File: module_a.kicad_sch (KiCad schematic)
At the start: 27 parts, among them J6 Micro_SD_Card_Det2, J7 nRPIBOOT Jumper, U3 TPD4EUSB30, U4 TPD4EUSB30, U5 MAX3232, U6 RT9742GGJ5

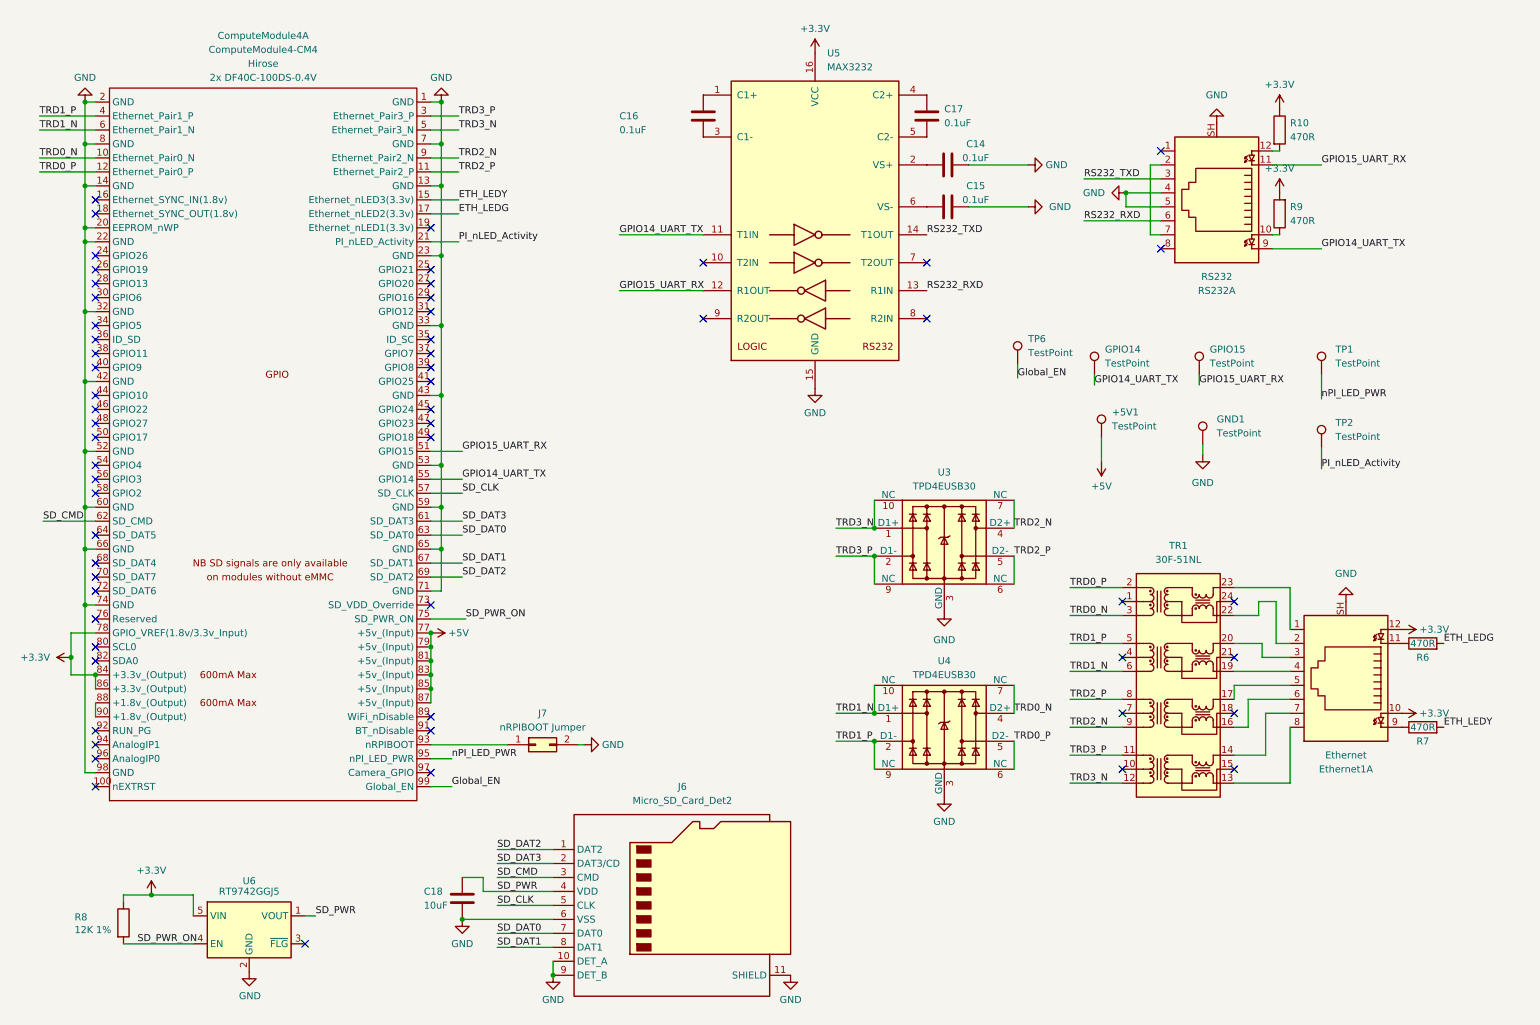
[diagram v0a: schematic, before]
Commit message: Fix ethernet wiring order
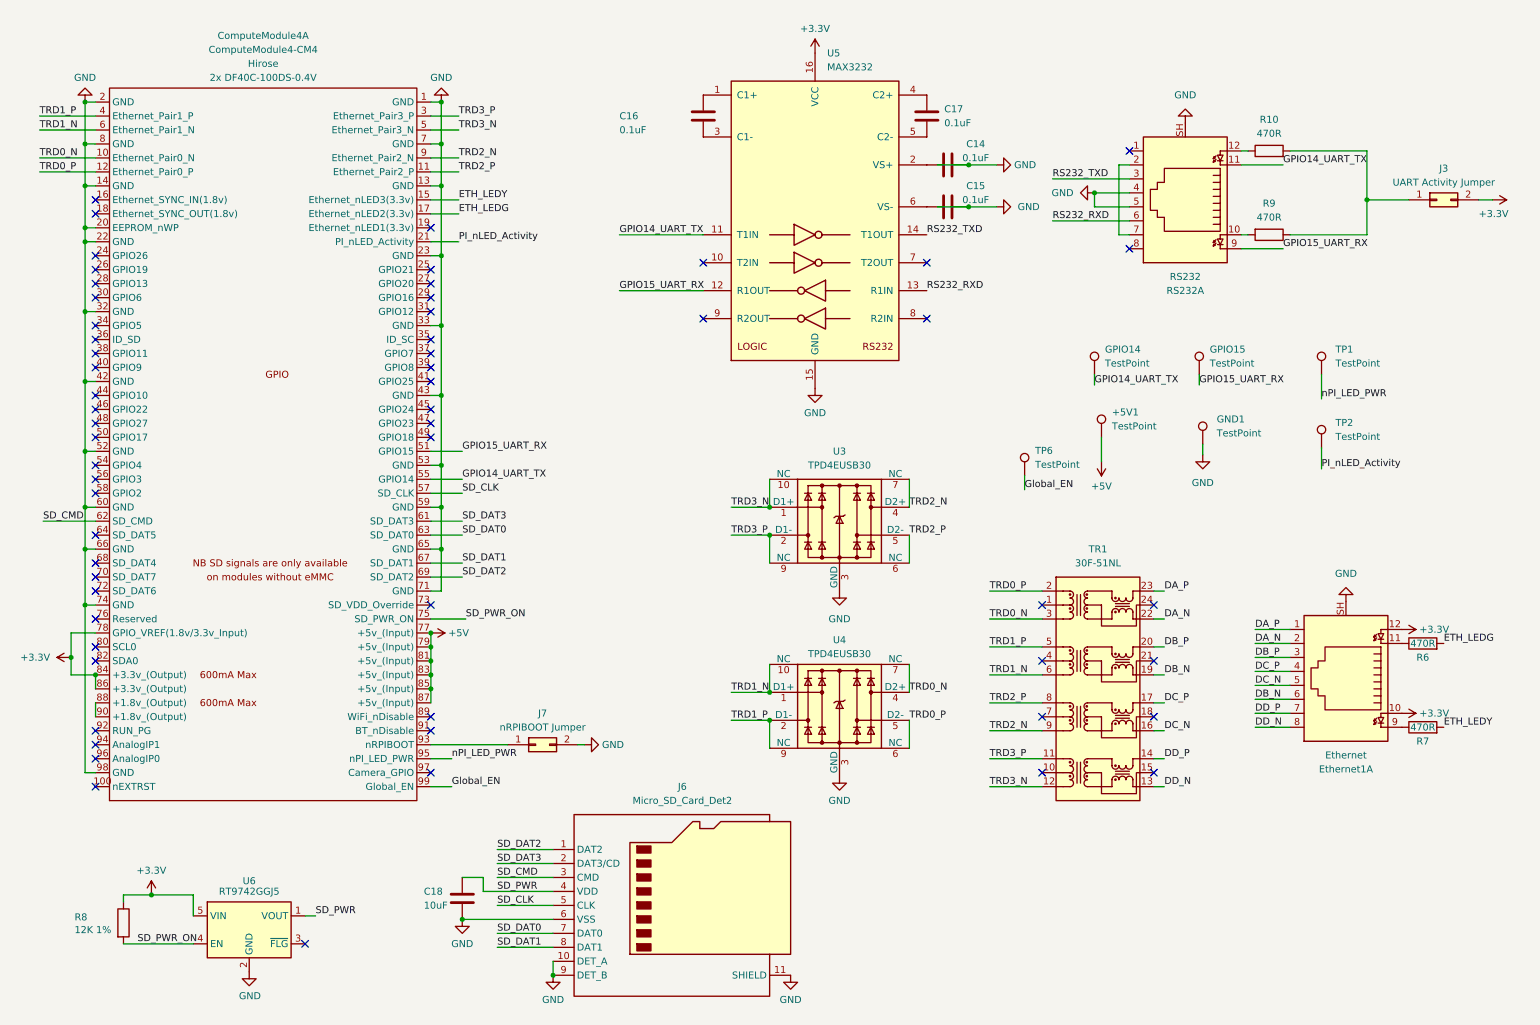
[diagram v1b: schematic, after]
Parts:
- added J3: UART Activity Jumper, Connector_PinHeader_2.00mm:PinHeader_1x02_P2.00mm_Vertical, symbol Connector_Generic:Conn_02x01
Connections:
- net +3.3V: now also J3.2 (Pin_2); no longer R10.1, R9.2
- net GPIO14_UART_TX: now also RS232.11; no longer RS232.9
- net GPIO15_UART_RX: now also RS232.9; no longer RS232.11
- net DA_P: now reaches Ethernet1.1, TR1.23 (MX1+)
- net DA_N: now reaches Ethernet1.2, TR1.22 (MX1-)
- net DB_P: now reaches Ethernet1.3, TR1.20 (MX2+)
- net DB_N: now reaches TR1.19 (MX2-)
- net DB_N: now also Ethernet1.6; no longer Ethernet1.4
- net DC_N: now reaches Ethernet1.5
- net DC_N: now also TR1.16 (MX3-); no longer TR1.17 (MX3+)
- net DD_P: now reaches Ethernet1.7, TR1.14 (MX4+)
- net DD_N: now reaches Ethernet1.8, TR1.13 (MX4-)
- net at RS232.10: now also R9.2; no longer R9.1
- net at RS232.12: now also R10.1; no longer R10.2
- new net: J3.1 (Pin_1), R10.2, R9.1
- new net DC_P: Ethernet1.4, TR1.17 (MX3+)
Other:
- moved on the sheet: R10, R9, RS232A, TP6, TR1, U3, U4

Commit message: Clean up schematics
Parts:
- C14, C15, C16, C17: value 0.1uF -> 100nF
- renumbered Ethernet1 to J5, RS232 to J8

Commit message: PiCard v2
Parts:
- removed +5V1, GND1, GPIO14, GPIO15, TP1, TP2, TP6: TestPoint, TestPoint:TestPoint_Pad_D2.0mm, symbol Connector:TestPoint
- removed J3: UART Activity Jumper, Connector_PinHeader_2.00mm:PinHeader_1x02_P2.00mm_Vertical, symbol Connector_Generic:Conn_02x01
- removed J7: nRPIBOOT Jumper, Connector_PinHeader_2.00mm:PinHeader_1x02_P2.00mm_Vertical, symbol Connector_Generic:Conn_02x01
- removed TR1: 30F-51NL, Transformer_SMD:Transformer_Ethernet_YDS_30F-51NL_SO-24_7.1x15.1mm, symbol Transformer:30F-51NL
- removed U6: RT9742GGJ5, Package_TO_SOT_SMD:TSOT-23-5, symbol PiCard:RT9742GGJ5F
- added C1, C34, C7: 100n, Capacitor_SMD:C_0402_1005Metric, symbol Device:C
- added C6, C8: 1u, Capacitor_SMD:C_0603_1608Metric, symbol Device:C
- added D1, D3: 1N5819WS, Diode_SMD:D_SOD-323, symbol Device:D_Schottky
- added D4: LED_Dual_AAKK, PiCard:LED-ARRAY-SMD_4P-L3.0-W1.5-L-FD, symbol Device:LED_Dual_AAKK
- added R21: 15.8k, Resistor_SMD:R_0402_1005Metric, symbol Device:R
- added R3, R36: 1k, Resistor_SMD:R_0402_1005Metric, symbol Device:R
- added R4, R5: 100k 1%, Resistor_SMD:R_0402_1005Metric, symbol Device:R
- added TR1: H2456G, PiCard:XFMR-SMD-24_L16.6-W9.0-LS9.6-BL, symbol Magi:H2456G
- added U18: 74LVC1G07, Package_TO_SOT_SMD:SOT-353_SC-70-5, symbol 74xGxx:74LVC1G07
- added U2: SN74AHC123A, Package_SO:TSSOP-16_4.4x5mm_P0.65mm, symbol 74xx:74AHCT123
- added U5: ~, Package_TO_SOT_SMD:SOT-23-6, symbol PiCard:TPS2553
- C2: renamed from C16; value 100nF -> 100n; footprint Capacitor_SMD:C_0603_1608Metric -> Capacitor_SMD:C_0402_1005Metric; LCSC C45000 -> C307331; MPN (none) -> CL05B104KB54PNC; Manufacturer (none) -> Samsung
- C3: renamed from C17; value 100nF -> 100n; footprint Capacitor_SMD:C_0603_1608Metric -> Capacitor_SMD:C_0402_1005Metric; LCSC C45000 -> C307331; MPN (none) -> CL05B104KB54PNC; Manufacturer (none) -> Samsung
- C4: renamed from C14; value 100nF -> 100n; footprint Capacitor_SMD:C_0603_1608Metric -> Capacitor_SMD:C_0402_1005Metric; LCSC C45000 -> C307331; MPN (none) -> CL05B104KB54PNC; Manufacturer (none) -> Samsung
- C5: renamed from C15; value 100nF -> 100n; footprint Capacitor_SMD:C_0603_1608Metric -> Capacitor_SMD:C_0402_1005Metric; LCSC C45000 -> C307331; MPN (none) -> CL05B104KB54PNC; Manufacturer (none) -> Samsung
- C9: renamed from C18; value 10uF -> 10u; LCSC C2167686 -> C15850; MPN (none) -> CL21A106KAYNNNE; Manufacturer (none) -> C15850
- J1: renamed from J8; footprint PiCard:RJ45-TH_MJ88B-B011-RVL11-P -> PiCard:RJ45-TH_RJ45-005-202-11; symbol Connector:RJ45_LED_Shielded_x2 -> Connector:RJ45_LED_Shielded; LCSC C501462 -> C7421405; MPN (none) -> RJ45-005-202-11; Manufacturer (none) -> Heling
- J2: renamed from J5; footprint PiCard:RJ45-TH_MJ88B-B011-RVL11-P -> PiCard:RJ45-TH_RJ45-005-202-11; symbol Connector:RJ45_LED_Shielded_x2 -> Connector:RJ45_LED_Shielded; LCSC C501462 -> C7421405; MPN (none) -> RJ45-005-202-11; Manufacturer (none) -> Heling
- J3: renamed from J6; LCSC (none) -> C5174683; LCSC Part # C5174683 -> (none); MPN (none) -> TF-108-ARP10; Manufacturer (none) -> XUNPU
- R1: renamed from R10; value 470R -> 470; footprint Resistor_SMD:R_0805_2012Metric -> Resistor_SMD:R_0402_1005Metric; LCSC C17710 -> C25117; MPN (none) -> 0402WGF4700TCE; Manufacturer (none) -> Uniroyal
- R2: renamed from R9; value 470R -> 470; footprint Resistor_SMD:R_0805_2012Metric -> Resistor_SMD:R_0402_1005Metric; LCSC C17710 -> C25117; MPN (none) -> 0402WGF4700TCE; Manufacturer (none) -> Uniroyal
- R6, R7: value 470R -> 470; footprint Resistor_SMD:R_0805_2012Metric -> Resistor_SMD:R_0402_1005Metric; LCSC C17710 -> C25117; MPN (none) -> 0402WGF4700TCE; Manufacturer (none) -> Uniroyal
- R8: value 12K 1% -> 12k; footprint Resistor_SMD:R_0805_2012Metric -> Resistor_SMD:R_0402_1005Metric; LCSC C17444 -> C25752; MPN (none) -> 0402WGF1202TCE; Manufacturer (none) -> Uniroyal
- U1: renamed from U5; footprint PiCard:TSSOP-16_L5.0-W4.4-P0.65-LS6.4-BL -> Package_SO:TSSOP-16_4.4x5mm_P0.65mm; MPN (none) -> MAX3232EEUE+T; Manufacturer (none) -> Maxim
- U3, U4: MPN (none) -> TPD4EUSB30DQAR; Manufacturer (none) -> Texas Instruments
- renumbered ComputeModule4 to ComputeModule1
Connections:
- net +3.3V: now also R8.2, C1.2, C34.2, C7.2, D1.1 (K), D3.1 (K), D4.1 (A1), D4.2 (A2), R4.1, R5.1, U18.5 (VCC), U2.10 (B), U2.16 (VCC), U2.2 (B), U5.1 (IN); no longer R8.1
- net DA_N: now also TR1.2 (MX1+)
- net DA_P: now also TR1.3 (MX1-)
- net DB_N: now also TR1.5 (MX2+)
- net DB_P: now also TR1.6 (MX2-)
- net DC_N: now also TR1.8 (MX3+)
- net DC_P: now also TR1.9 (MX3-)
- net DD_N: now also TR1.11 (MX4+)
- net DD_P: now also TR1.12 (MX4-)
- net GND: now also J1.11, J1.9, C1.1, C34.1, C6.2, C7.1, C8.2, R21.2, U18.3 (GND), U2.14 (Cext), U2.6 (Cext), U2.8 (GND), U5.2 (GND); no longer ComputeModule1.98 (GND)
- net GPIO14_UART_TX: now also U2.1 (A); no longer J1.11
- net GPIO15_UART_RX: now also U2.9 (A); no longer J1.9
- net SD_PWR: now also U5.6 (OUT)
- net SD_PWR_ON: now also R8.1, U5.3 (EN); no longer R8.2
- net TRD0_N: now also U4.1 (D1+), U4.10 (NC), TR1.23 (TD1+); no longer U4.4 (D2+), U4.7 (NC)
- net TRD0_P: now also U4.2 (D1-), U4.9 (NC), TR1.22 (TD1-); no longer U4.5 (D2-), U4.6 (NC)
- net TRD1_N: now also U4.4 (D2+), U4.7 (NC), TR1.20 (TD2+); no longer U4.1 (D1+), U4.10 (NC)
- net TRD1_P: now also U4.5 (D2-), U4.6 (NC), TR1.19 (TD2-); no longer U4.2 (D1-), U4.9 (NC)
- net TRD2_N: now also U3.5 (D2-), U3.6 (NC), TR1.17; no longer U3.4 (D2+), U3.7 (NC)
- net TRD2_P: now also U3.4 (D2+), U3.7 (NC), TR1.16 (TD3-); no longer U3.5 (D2-), U3.6 (NC)
- net TRD3_N: now also U3.2 (D1-), U3.9 (NC), TR1.14 (TD4+); no longer U3.1 (D1+), U3.10 (NC)
- net TRD3_P: now also U3.1 (D1+), U3.10 (NC), TR1.13 (TD4-); no longer U3.2 (D1-), U3.9 (NC)
- net RTC_SCL: now reaches ComputeModule1.56 (GPIO3)
- net RTC_SDA: now reaches ComputeModule1.58 (GPIO2)
- net RPIBOOT: now reaches ComputeModule1.93 (nRPIBOOT)
- net UART_RX_ACT: now reaches R2.1
- net UART_RX_ACT: now also U2.5 (Q); no longer R1.2
- net Global_EN: no longer names the net of ComputeModule1.99 (Global_EN)
- net PI_nLED_Activity renamed GREEN_LED_K
- net GREEN_LED_K: now also R3.1
- net nPI_LED_PWR: no longer names the net of ComputeModule1.95 (nPI_LED_PWR)
- net nPI_LED_PWR: now also U18.2
- new net: R21.1, U5.5 (ILM)
- new net: C6.1, D1.2 (A), R4.2, U2.15 (RCext)
- new net: C8.1, D3.2 (A), R5.2, U2.7 (RCext)
- new net: D4.3 (K1), R36.2
- new net: D4.4 (K2), R3.2
- new net RED_LED_K: R36.1, U18.4
- new net UART_ACT_EN: U2.11 (Clr), U2.3 (Clr)
- new net UART_TX_ACT: R1.2, U2.13 (Q)
- no-connect marks 59 -> 62
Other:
- moved on the sheet: C9, ComputeModule1A, J1, J3, R1, R2, U3, U4

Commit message: PiCard v2.2
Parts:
- U5: value ~ -> TPS2553
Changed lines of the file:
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@@
 			)
 		)
-		(property "Value" "~"
+		(property "Value" "TPS2553"
 			(at 45.72 170.815 0)
 			(effects

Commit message: wip
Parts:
- removed C5: 100n, Capacitor_SMD:C_0402_1005Metric, symbol Device:C
- removed D4: LED_Dual_AAKK, PiCard:LED-ARRAY-SMD_4P-L3.0-W1.5-L-FD, symbol Device:LED_Dual_AAKK
- removed R3, R36: 1k, Resistor_SMD:R_0402_1005Metric, symbol Device:R
- removed U1: MAX3232, Package_SO:TSSOP-16_4.4x5mm_P0.65mm, symbol Interface_UART:MAX3232
- removed U18: 74LVC1G07, Package_TO_SOT_SMD:SOT-353_SC-70-5, symbol 74xGxx:74LVC1G07
- added U1: ADM3101EACPZ, PiCard:LFCSP-12-1EP_3x3mm_P0.5mm_EP1.3x1.3mm, symbol PiCard:ADM3101EACPZ
- U2: footprint Package_SO:TSSOP-16_4.4x5mm_P0.65mm -> Package_DFN_QFN:DHVQFN-16-1EP_2.5x3.5mm_P0.5mm_EP1x2mm
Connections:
- net +3.3V: no longer C1.2
- net GND: now also U1.13 (GND), U1.6 (GND); no longer C1.1
- net GPIO14_UART_TX: now also U1.3 (TIN)
- net GPIO15_UART_RX: now also U1.2 (ROUT)
- net RS232_RXD: now also U1.8 (TOUT)
- net RS232_TXD: now also U1.9 (RIN)
- net at C2.1: now also U1.11 (C2+)
- net at C4.1: now also U1.7 (V-)
- net at C2.2: now also U1.10 (C2-)
- net at C3.1: now also U1.5 (VCC)
- net at C3.2: now also U1.4 (V+)
- new net: C1.1, U1.1 (C1+)
- new net: C1.2, U1.12 (C1-)
- no-connect marks 62 -> 57
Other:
- moved on the sheet: C6, C7, C8, D1, D3, J1, J2, R1, R2, R4, R5, R6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

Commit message: wip2
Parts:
- U2: value SN74AHC123A -> 74AHCT123ABQ; LCSC C2869599 -> C554491; MPN SN74AHC123APWR -> 74AHCT123ABQ,115; Manufacturer Texas Instruments -> Nexperia
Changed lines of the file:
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@@
 			)
 		)
-		(property "Value" "SN74AHC123A"
+		(property "Value" "74AHCT123ABQ"
 			(at 268.605 83.82 0)
 			(effects
@@
 			)
 		)
-		(property "Datasheet" "https://www.ti.com/lit/ds/symlink/sn74ahc123a.pdf"
+		(property "Datasheet" "https://assets.nexperia.com/documents/data-sheet/74AHC_AHCT123A.pdf"
 			(at 261.62 82.55 0)
 			(effects
@@
 			)
 		)
-		(property "LCSC" "C2869599"
+		(property "LCSC" "C554491"
 			(at 261.62 82.55 0)
 			(effects
@@
 			)
 		)
-		(property "MPN" "SN74AHC123APWR"
+		(property "MPN" "74AHCT123ABQ,115"
 			(at 261.62 82.55 0)
 			(effects
@@
 			)
 		)
-		(property "Manufacturer" "Texas Instruments"
+		(property "Manufacturer" "Nexperia"
 			(at 261.62 82.55 0)
 			(effects
@@
 			)
 		)
-		(property "Value" "SN74AHC123A"
+		(property "Value" "74AHCT123ABQ"
 			(at 228.6 76.2 0)
 			(effects
@@
 			)
 		)
-		(property "Datasheet" "https://www.ti.com/lit/ds/symlink/sn74ahc123a.pdf"
+		(property "Datasheet" "https://assets.nexperia.com/documents/data-sheet/74AHC_AHCT123A.pdf"
 			(at 228.6 86.36 0)
 			(effects
@@
 			)
 		)
-		(property "LCSC" "C2869599"
+		(property "LCSC" "C554491"
 			(at 228.6 86.36 0)
 			(effects
@@
 			)
 		)
-		(property "MPN" "SN74AHC123APWR"
+		(property "MPN" "74AHCT123ABQ,115"
 			(at 228.6 86.36 0)
 			(effects
@@
 			)
 		)
-		(property "Manufacturer" "Texas Instruments"
+		(property "Manufacturer" "Nexperia"
 			(at 228.6 86.36 0)
 			(effects
@@
 			)
 		)
-		(property "Value" "SN74AHC123A"
+		(property "Value" "74AHCT123ABQ"
 			(at 165.1 76.835 0)
 			(effects
@@
 			)
 		)
-		(property "Datasheet" "https://www.ti.com/lit/ds/symlink/sn74ahc123a.pdf"
+		(property "Datasheet" "https://assets.nexperia.com/documents/data-sheet/74AHC_AHCT123A.pdf"
 			(at 165.1 86.36 0)
 			(effects
@@
 			)
 		)
-		(property "LCSC" "C2869599"
+		(property "LCSC" "C554491"
 			(at 165.1 86.36 0)
 			(effects
@@
 			)
 		)
-		(property "MPN" "SN74AHC123APWR"
+		(property "MPN" "74AHCT123ABQ,115"
 			(at 165.1 86.36 0)
 			(effects
@@
 			)
 		)
-		(property "Manufacturer" "Texas Instruments"
+		(property "Manufacturer" "Nexperia"
 			(at 165.1 86.36 0)
 			(effects

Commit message: wip3
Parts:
- removed C34: 100n, Capacitor_SMD:C_0402_1005Metric, symbol Device:C
- removed R21: 15.8k, Resistor_SMD:R_0402_1005Metric, symbol Device:R
- removed U5: TPS2553, Package_TO_SOT_SMD:SOT-23-6, symbol PiCard:TPS2553
- added U18: TPS2069C, Package_TO_SOT_SMD:SOT-23-5, symbol PiCard:TPS2069C
- J3: footprint PiCard:TF-SMD_503398-1892 -> PiCard:SDCARD_MOLEX_503398-1892; LCSC C5174683 -> C428492; MPN TF-108-ARP10 -> 5033981892; Manufacturer XUNPU -> MOLEX
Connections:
- net +3.3V: now also U18.5 (IN)
- net GND: now also U18.2 (GND)
- net RS232_RXD: now also U1.9 (RIN); no longer U1.8 (TOUT)
- net RS232_TXD: now also U1.8 (TOUT); no longer U1.9 (RIN)
- net SD_PWR: now also U18.1 (OUT)
- net SD_PWR_ON: now also U18.4 (EN)
- net MCU_nRST: now reaches ComputeModule1.24 (GPIO26)
- net CM_SPI1_SCLK: now reaches ComputeModule1.25 (GPIO21)
- net CM_SPI1_SIO1: now reaches ComputeModule1.26 (GPIO19)
- net CM_SPI1_SIO0: now reaches ComputeModule1.27 (GPIO20)
- net CM_UART4_RX: now reaches ComputeModule1.28 (GPIO13)
- net MCU_SWDCLK: now reaches ComputeModule1.30 (GPIO6)
- net CM_UART4_TX: now reaches ComputeModule1.31 (GPIO12)
- net CM_I2C2_SCL: now reaches ComputeModule1.34 (GPIO5)
- net CM_ID_SC: now reaches ComputeModule1.35 (ID_SC)
- net CM_ID_SD: now reaches ComputeModule1.36 (ID_SD)
- net MCU_SWDIO: now reaches ComputeModule1.37 (GPIO7)
- net CM_UART3_TX: now reaches ComputeModule1.39 (GPIO8)
- net CM_UART3_RX: now reaches ComputeModule1.40 (GPIO9)
- net CM_SPI1_CSN0: now reaches ComputeModule1.49 (GPIO18)
- net CM_I2C2_SDA: now reaches ComputeModule1.54 (GPIO4)
- net CM_PWR_BUTTON: now reaches ComputeModule1.92 (RUN_PG)
- net RTC_SCL renamed CM_I2C1_SCL
- net RTC_SDA renamed CM_I2C1_SDA
- no-connect marks 57 -> 41
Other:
- moved on the sheet: C6, C8, C9, ComputeModule1A, D1, D3, J2, J3, R4, R5, R6, R7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

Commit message: WIP
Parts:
- added C51: 100n, Capacitor_SMD:C_0402_1005Metric, symbol Device:C
- C8: renamed from C9; Manufacturer C15850 -> Samsung
- ComputeModule1: symbol PiCard:ComputeModule4-CM4 -> PiCard:ComputeModule5-CM5; Field4 Hirose -> Amphenol; Field5 2x DF40C-100DS-0.4V -> 2x 10164227-1001A1RLF
- U2: value 74AHCT123ABQ -> 74HC123PW; footprint Package_DFN_QFN:DHVQFN-16-1EP_2.5x3.5mm_P0.5mm_EP1x2mm -> Package_SO:TSSOP-16_4.4x5mm_P0.65mm; LCSC C554491 -> C426698; MPN 74AHCT123ABQ,115 -> 74HC123PW,118
- U5: renamed from U18; LCSC (none) -> C181752; MPN (none) -> TPS2069CDBVR; Manufacturer (none) -> Texas Instruments
- renumbered C3 to C2, C4 to C3, C2 to C4, C7 to C5, C8 to C6, C6 to C7, D3 to D2, R5 to R3, R6 to R5, R7 to R6, R8 to R7
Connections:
- net +3.3V: now also C2.1, U1.5 (VCC), C51.1
- net DA_N: now also TR1.8 (MX3+); no longer TR1.2 (MX1+)
- net DA_P: now also TR1.9 (MX3-); no longer TR1.3 (MX1-)
- net DB_N: now also TR1.11 (MX4+); no longer TR1.5 (MX2+)
- net DB_P: now also TR1.12 (MX4-); no longer TR1.6 (MX2-)
- net DC_N: now also TR1.5 (MX2+); no longer TR1.8 (MX3+)
- net DC_P: now also TR1.6 (MX2-); no longer TR1.9 (MX3-)
- net DD_N: now also TR1.2 (MX1+); no longer TR1.11 (MX4+)
- net DD_P: now also TR1.3 (MX1-); no longer TR1.12 (MX4-)
- net GND: now also C51.2
- net MCU_nRST: now also ComputeModule1.38 (GPIO11); no longer ComputeModule1.24 (GPIO26)
- net TRD0_N: now also TR1.17, U4.2 (D1-), U4.9 (NC); no longer TR1.23 (TD1+), U4.1 (D1+), U4.10 (NC)
- net TRD0_P: now also TR1.16 (TD3-), U4.1 (D1+), U4.10 (NC); no longer TR1.22 (TD1-), U4.2 (D1-), U4.9 (NC)
- net TRD1_N: now also TR1.14 (TD4+); no longer TR1.20 (TD2+)
- net TRD1_P: now also TR1.13 (TD4-); no longer TR1.19 (TD2-)
- net TRD2_N: now also TR1.20 (TD2+), U3.4 (D2+), U3.7 (NC); no longer TR1.17, U3.5 (D2-), U3.6 (NC)
- net TRD2_P: now also TR1.19 (TD2-), U3.5 (D2-), U3.6 (NC); no longer TR1.16 (TD3-), U3.4 (D2+), U3.7 (NC)
- net TRD3_N: now also TR1.23 (TD1+); no longer TR1.14 (TD4+)
- net TRD3_P: now also TR1.22 (TD1-); no longer TR1.13 (TD4-)
- net CM_PWR_EN: now reaches ComputeModule1.48 (GPIO27)
- net CM_PWR_LED: now reaches ComputeModule1.95 (LED_nPWR)
- net GREEN_LED_K renamed CM_ACT_LED
- no-connect marks 41 -> 40
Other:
- title: (none) -> PiCard
- moved on the sheet: TR1
